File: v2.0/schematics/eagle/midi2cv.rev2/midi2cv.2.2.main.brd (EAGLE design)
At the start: 99.4 x 41.9 mm, 36 parts, among them IC1 PIC18F2431DIP, Q1 20MHz, X1 MAB5SH

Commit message: Corrected pin mappings on Jacks Updated midi2cv with new jacks mapping Rerouted main and pnl Increased minimum width in design rules from 6mil to 12mil
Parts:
- flipped S1 to the bottom
- flipped SV1 to the bottom
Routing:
- net N$1: track 8.77 -> 28.3 mm
- net N$11: track 46.1 -> 34.0 mm
- net N$19: track 56.5 -> 46.5 mm
- net CV2: track 43.5 -> 35.6 mm
- net VPP: track 67.6 -> 60.1 mm
- net 0V: track 215.3 -> 222.2 mm
- net N$20: track 28.8 -> 22.7 mm
- net N$9: track 22.6 -> 28.5 mm
- net CV3: track 34.3 -> 28.9 mm
- net GATE4: track 17.5 -> 12.4 mm
- net +12V: track 56.5 -> 61.0 mm
- net N$10: track 33.0 -> 37.4 mm
- net N$28: track 59.0 -> 54.7 mm
- net N$13: track 38.0 -> 35.2 mm
- net PGD: track 13.5 -> 16.2 mm
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
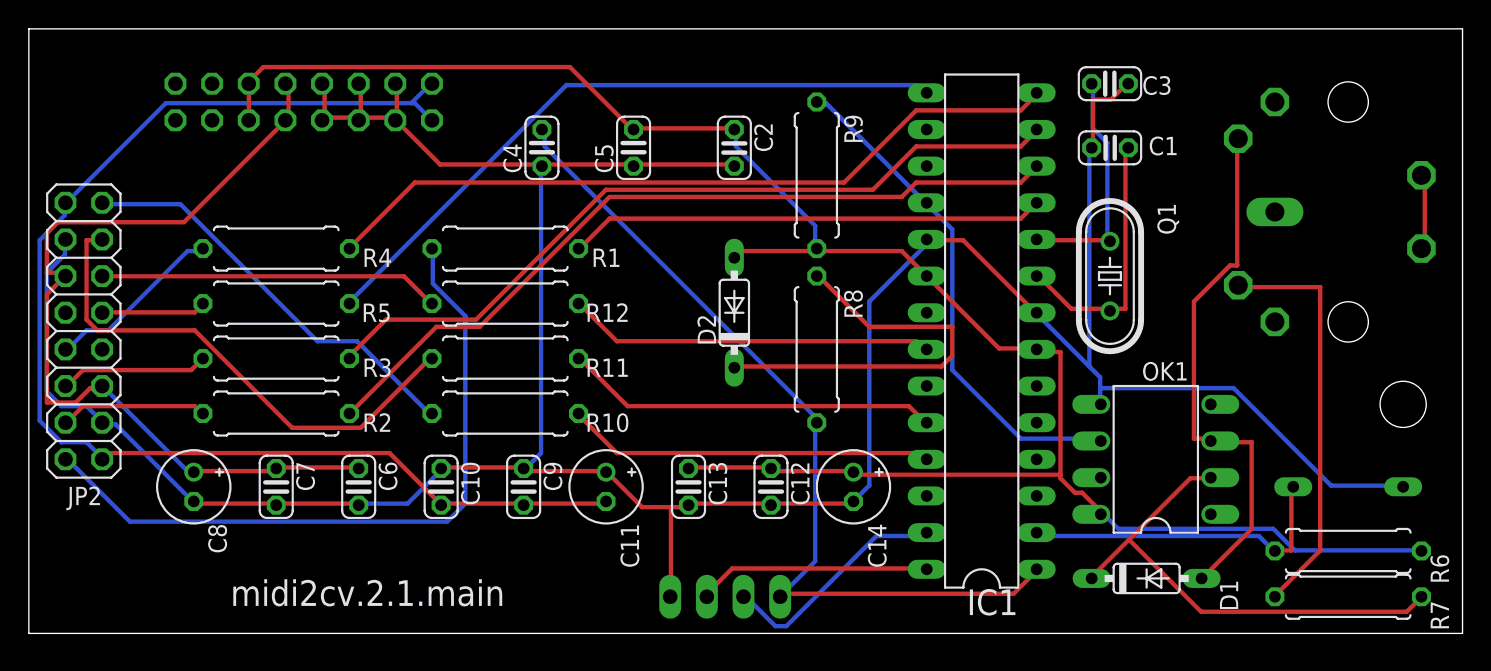
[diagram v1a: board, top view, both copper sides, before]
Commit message: Roated midi jack
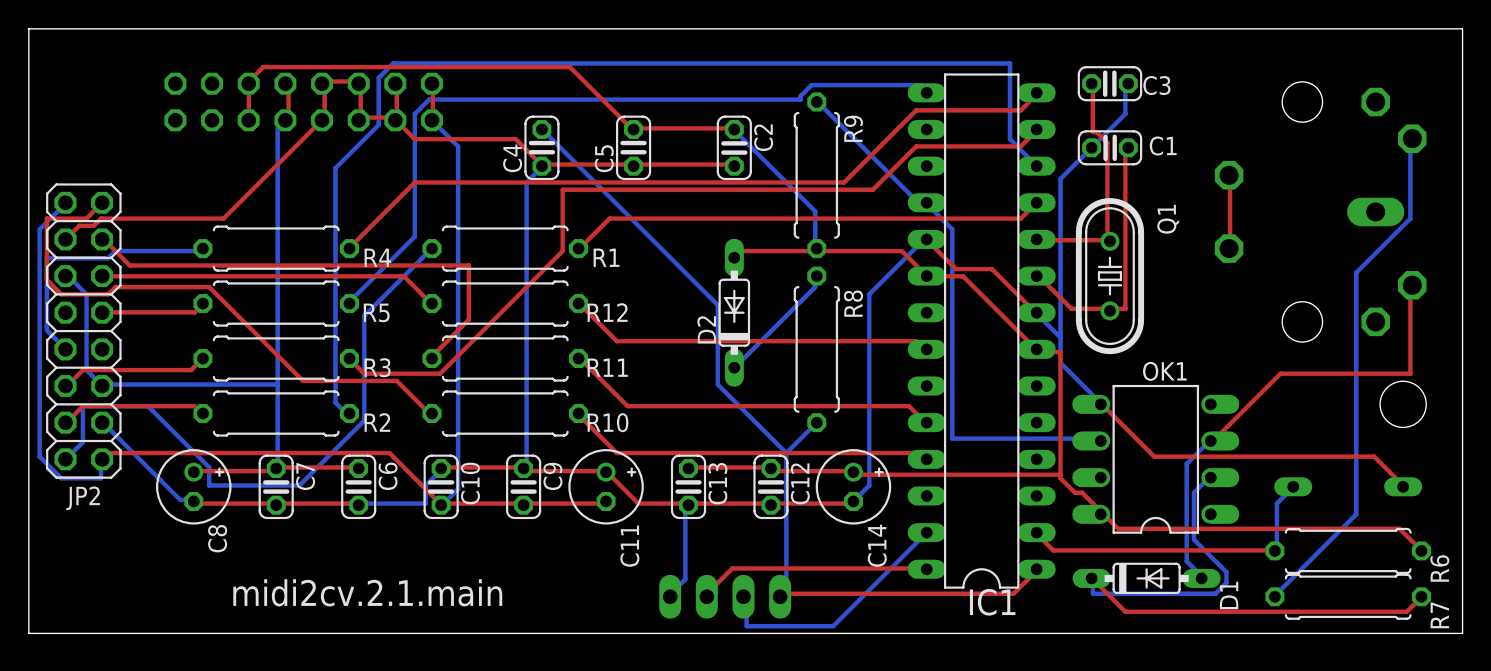
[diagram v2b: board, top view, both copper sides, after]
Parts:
- moved X1 3.17 mm to (88.3, 29.2), turned to 90 degrees
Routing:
- net N$28: track 54.7 -> 77.1 mm
- net N$1: track 28.3 -> 8.77 mm
- net CV3: track 28.9 -> 39.5 mm
- net N$11: track 34.0 -> 43.7 mm
- net N$9: track 28.5 -> 35.7 mm
- net GATE1: track 48.6 -> 42.4 mm
- net GATE4: track 12.4 -> 18.0 mm
- net N$19: track 46.5 -> 52.0 mm
- net N$10: track 37.4 -> 32.7 mm
- net 0V: track 222.2 -> 226.6 mm
- net N$29: track 54.3 -> 57.6 mm
- net -12V: track 88.9 -> 91.9 mm
- net N$13: track 35.2 -> 38.0 mm
- net CV2: track 35.6 -> 33.6 mm
- net +12V: track 61.0 -> 59.7 mm
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
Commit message: Updated version on schem and board to 2.2 Revised labels for GATE1..5 to match board layout and firmare
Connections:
- net GATE1: now also JP2.9, R5.2; no longer JP2.2, R1.1
- net GATE2: now also JP2.8, R4.1; no longer JP2.4, R2.1
- net GATE4: now also JP2.4, R2.1; no longer JP2.8, R4.1
- net GATE5: now also JP2.2, R1.1; no longer JP2.9, R5.2
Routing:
- net GATE1: track 42.4 -> 7.13 mm
- net GATE5: track 7.26 -> 42.2 mm
- net GATE4: track 18.0 -> 10.1 mm
- net GATE2: track 10.2 -> 17.8 mm
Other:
- board text added: "midi2cv.2.2.main"
- board text removed: "midi2cv.2.1.main"
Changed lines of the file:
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@@
 <wire x1="99.365" y1="41.9" x2="0" y2="41.9" width="0" layer="20"/>
 <wire x1="0" y1="41.9" x2="0" y2="0" width="0" layer="20"/>
-<text x="13.97" y="1.905" size="1.778" layer="25" font="vector">midi2cv.2.1.main</text>
+<text x="13.97" y="1.905" size="1.778" layer="25" font="vector">midi2cv.2.2.main</text>
 <hole x="95.25" y="15.875" drill="3.2"/>
 </plain>
@@
 <wire x1="86.5" y1="5.75" x2="86.36" y2="5.715" width="0.3048" layer="16"/>
 </signal>
-<signal name="GATE1">
-<contactref element="JP2" pad="2"/>
-<contactref element="R1" pad="1"/>
-<wire x1="23.25" y1="22" x2="27.75" y2="26.5" width="0.3048" layer="16"/>
-<wire x1="23.25" y1="14.75" x2="23.25" y2="22" width="0.3048" layer="16"/>
-<wire x1="18.75" y1="10.25" x2="23.25" y2="14.75" width="0.3048" layer="16"/>
-<wire x1="12.5" y1="10.25" x2="18.75" y2="10.25" width="0.3048" layer="16"/>
-<wire x1="12.5" y1="11.5" x2="12.5" y2="10.25" width="0.3048" layer="16"/>
-<wire x1="8.25" y1="15.75" x2="12.5" y2="11.5" width="0.3048" layer="16"/>
-<wire x1="3.75" y1="15.75" x2="8.25" y2="15.75" width="0.3048" layer="16"/>
-<wire x1="3.75" y1="13.25" x2="3.75" y2="15.75" width="0.3048" layer="16"/>
-<wire x1="2.75" y1="12.25" x2="3.75" y2="13.25" width="0.3048" layer="16"/>
-<wire x1="27.75" y1="26.5" x2="27.94" y2="26.67" width="0.3048" layer="16"/>
-<wire x1="2.75" y1="12.25" x2="2.54" y2="12.065" width="0.3048" layer="16"/>
-</signal>
-<signal name="GATE2">
-<contactref element="JP2" pad="4"/>
-<contactref element="R2" pad="1"/>
-<wire x1="11.5" y1="15.75" x2="12" y2="15.25" width="0.3048" layer="1"/>
-<wire x1="3.75" y1="15.75" x2="11.5" y2="15.75" width="0.3048" layer="1"/>
-<wire x1="2.75" y1="14.75" x2="3.75" y2="15.75" width="0.3048" layer="1"/>
-<wire x1="12" y1="15.25" x2="12.065" y2="15.24" width="0.3048" layer="1"/>
-<wire x1="2.75" y1="14.75" x2="2.54" y2="14.605" width="0.3048" layer="1"/>
-</signal>
 <signal name="GATE3">
 <contactref element="JP2" pad="6"/>
@@
 <wire x1="12" y1="19" x2="12.065" y2="19.05" width="0.3048" layer="1"/>
 <wire x1="2.75" y1="17.25" x2="2.54" y2="17.145" width="0.3048" layer="1"/>
-</signal>
-<signal name="GATE4">
-<contactref element="JP2" pad="8"/>
-<contactref element="R4" pad="1"/>
-<wire x1="6" y1="26.5" x2="12" y2="26.5" width="0.3048" layer="16"/>
-<wire x1="5.5" y1="26" x2="6" y2="26.5" width="0.3048" layer="16"/>
-<wire x1="1.25" y1="26" x2="5.5" y2="26" width="0.3048" layer="16"/>
-<wire x1="1.25" y1="21" x2="1.25" y2="26" width="0.3048" layer="16"/>
-<wire x1="2.5" y1="19.75" x2="1.25" y2="21" width="0.3048" layer="16"/>
-<wire x1="12" y1="26.5" x2="12.065" y2="26.67" width="0.3048" layer="16"/>
-<wire x1="2.5" y1="19.75" x2="2.54" y2="19.685" width="0.3048" layer="16"/>
-</signal>
-<signal name="GATE5">
-<contactref element="JP2" pad="9"/>
-<contactref element="R5" pad="2"/>
-<wire x1="11.5" y1="22.25" x2="12" y2="22.75" width="0.3048" layer="1"/>
-<wire x1="5.25" y1="22.25" x2="11.5" y2="22.25" width="0.3048" layer="1"/>
-<wire x1="12" y1="22.75" x2="12.065" y2="22.86" width="0.3048" layer="1"/>
-<wire x1="5.25" y1="22.25" x2="5.08" y2="22.225" width="0.3048" layer="1"/>
 </signal>
 <signal name="CV2">
@@
 <wire x1="5.25" y1="24.75" x2="5.08" y2="24.765" width="0.3048" layer="1"/>
 </signal>
+<signal name="GATE5">
+<contactref element="R1" pad="1"/>
+<contactref element="JP2" pad="2"/>
+<wire x1="23.25" y1="22" x2="27.75" y2="26.5" width="0.3048" layer="16"/>
+<wire x1="23.25" y1="14.75" x2="23.25" y2="22" width="0.3048" layer="16"/>
+<wire x1="18.75" y1="10.25" x2="23.25" y2="14.75" width="0.3048" layer="16"/>
+<wire x1="12.5" y1="10.25" x2="18.75" y2="10.25" width="0.3048" layer="16"/>
+<wire x1="12.5" y1="11.5" x2="12.5" y2="10.25" width="0.3048" layer="16"/>
+<wire x1="8.25" y1="15.75" x2="12.5" y2="11.5" width="0.3048" layer="16"/>
+<wire x1="3.75" y1="15.75" x2="8.25" y2="15.75" width="0.3048" layer="16"/>
+<wire x1="3.75" y1="13.25" x2="3.75" y2="15.75" width="0.3048" layer="16"/>
+<wire x1="2.75" y1="12.25" x2="3.75" y2="13.25" width="0.3048" layer="16"/>
+<wire x1="2.75" y1="12.25" x2="2.54" y2="12.065" width="0.3048" layer="16"/>
+<wire x1="27.75" y1="26.5" x2="27.94" y2="26.67" width="0" layer="19" extent="16-16"/>
+</signal>
+<signal name="GATE4">
+<contactref element="R2" pad="1"/>
+<contactref element="JP2" pad="4"/>
+<wire x1="11.5" y1="15.75" x2="12" y2="15.25" width="0.3048" layer="1"/>
+<wire x1="3.75" y1="15.75" x2="11.5" y2="15.75" width="0.3048" layer="1"/>
+<wire x1="2.75" y1="14.75" x2="3.75" y2="15.75" width="0.3048" layer="1"/>
+<wire x1="2.75" y1="14.75" x2="2.54" y2="14.605" width="0.3048" layer="1"/>
+<wire x1="12" y1="15.25" x2="12.065" y2="15.24" width="0" layer="19" extent="1-1"/>
+</signal>
+<signal name="GATE2">
+<contactref element="R4" pad="1"/>
+<contactref element="JP2" pad="8"/>
+<wire x1="6" y1="26.5" x2="12" y2="26.5" width="0.3048" layer="16"/>
+<wire x1="5.5" y1="26" x2="6" y2="26.5" width="0.3048" layer="16"/>
+<wire x1="1.25" y1="26" x2="5.5" y2="26" width="0.3048" layer="16"/>
+<wire x1="1.25" y1="21" x2="1.25" y2="26" width="0.3048" layer="16"/>
+<wire x1="2.5" y1="19.75" x2="1.25" y2="21" width="0.3048" layer="16"/>
+<wire x1="2.5" y1="19.75" x2="2.54" y2="19.685" width="0.3048" layer="16"/>
+<wire x1="12" y1="26.5" x2="12.065" y2="26.67" width="0" layer="19" extent="16-16"/>
+</signal>
+<signal name="GATE1">
+<contactref element="R5" pad="2"/>
+<contactref element="JP2" pad="9"/>
+<wire x1="11.5" y1="22.25" x2="12" y2="22.75" width="0.3048" layer="1"/>
+<wire x1="5.25" y1="22.25" x2="11.5" y2="22.25" width="0.3048" layer="1"/>
+<wire x1="5.25" y1="22.25" x2="5.08" y2="22.225" width="0.3048" layer="1"/>
+<wire x1="12" y1="22.75" x2="12.065" y2="22.86" width="0" layer="19" extent="1-1"/>
+</signal>
 </signals>
